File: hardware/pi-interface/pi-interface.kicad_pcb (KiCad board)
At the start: 2 copper layers, 8 parts, among them J1 RasPI_IO_Header, P1 SL030 RFID, P2 Molex HDD Power, P3 Door Solenoid, Q1 BC237

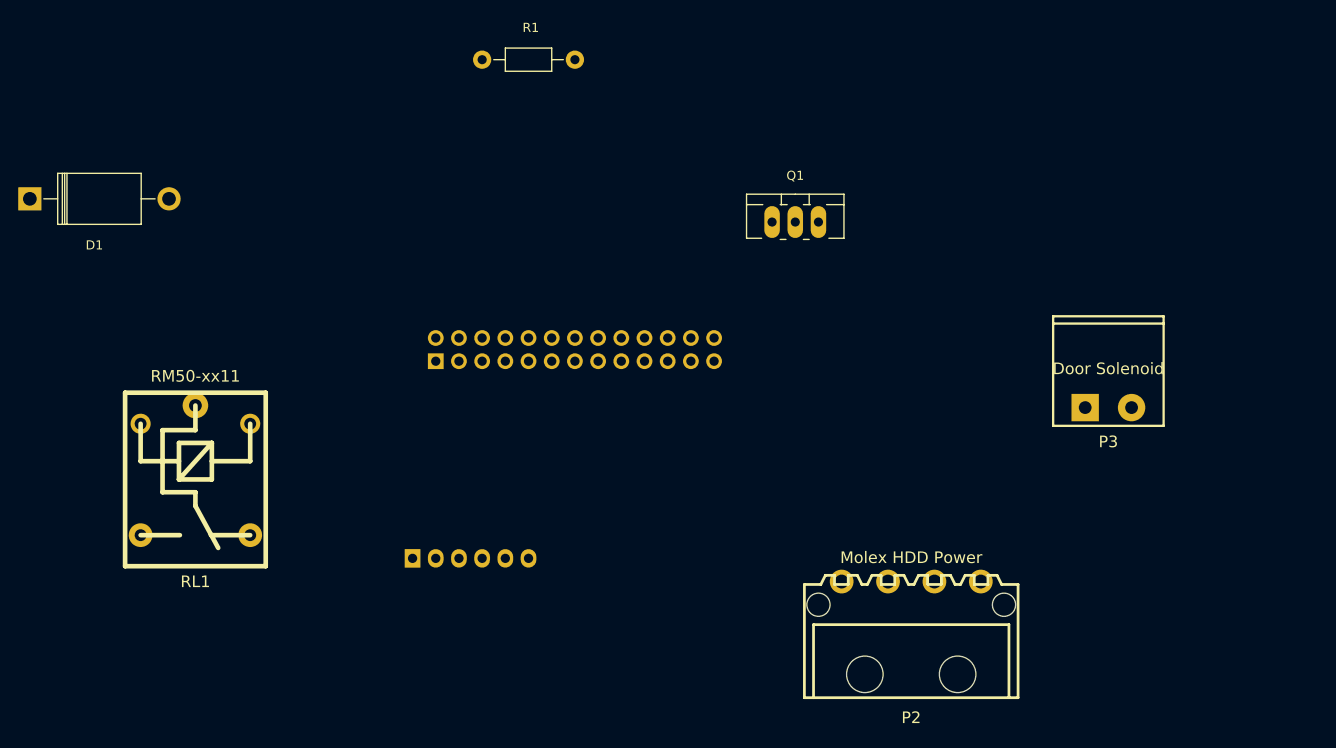
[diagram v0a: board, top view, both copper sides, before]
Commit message: Improved PCB, still needs checking against parts ordered
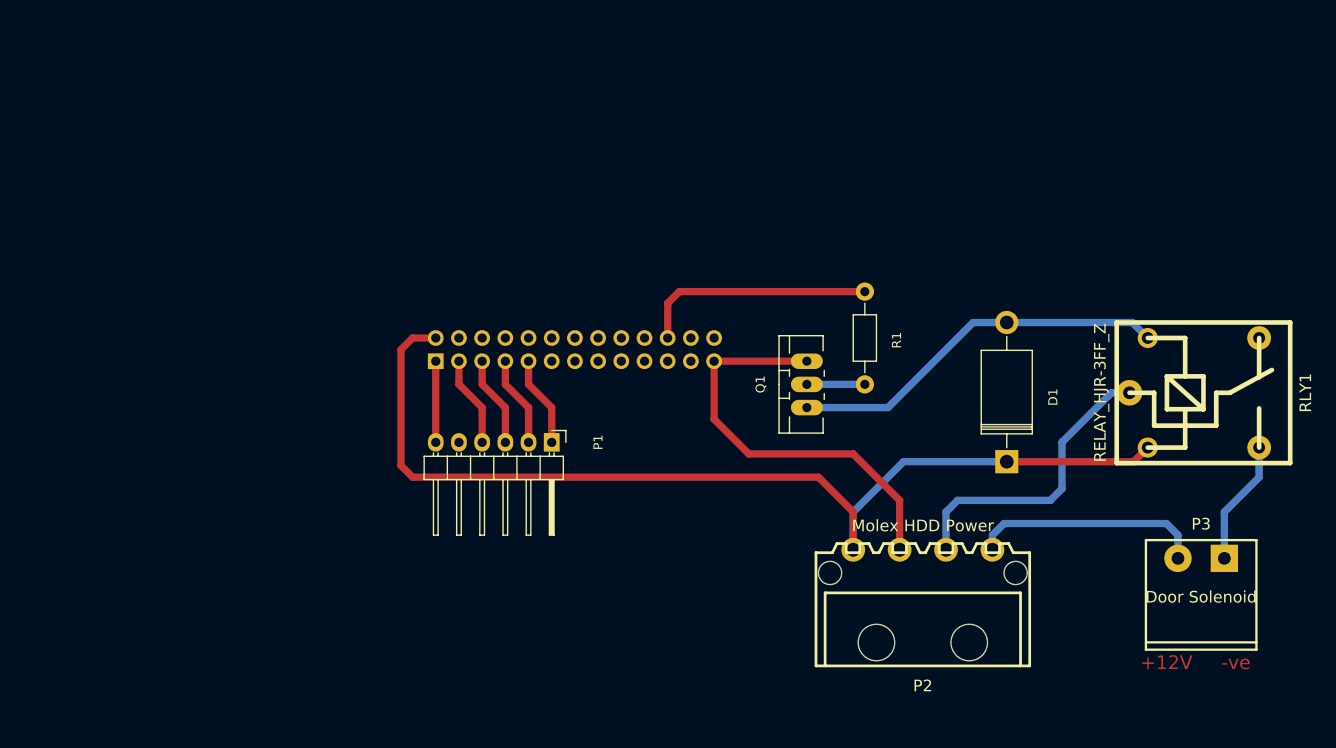
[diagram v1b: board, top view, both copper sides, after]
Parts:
- removed RL1: RM50-xx11, w_relay:relay_hjr-3ff_z
- added RLY1: RELAY_HJR-3FF_Z, w_relay:relay_hjr-3ff_z, F.Cu at (251.7, 98.7)
- P1: moved to F.Cu
- R1: value R -> 220R
- moved D1 110.8 mm to (230.2, 106.3), turned to 90 degrees
- moved R1 47.8 mm to (214.6, 92.7), turned to 270 degrees
- moved P1 19.8 mm to (180.3, 104.1)
- moved P3 19.4 mm to (251.5, 116.8), turned to 180 degrees
- moved Q1 17.8 mm to (208.3, 97.8), turned to 90 degrees
- moved P2 3.70 mm to (221.0, 121.9)
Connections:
- P1 pad 1: Net-(J1-Pad1) -> Net-(J1-Pad9)
- P1 pad 2: Net-(P1-Pad2) -> Net-(J1-Pad7)
- P1 pad 3: Net-(J1-Pad3) -> Net-(J1-Pad5)
- P1 pad 4: Net-(J1-Pad5) -> Net-(J1-Pad3)
- P1 pad 5: Net-(J1-Pad7) -> Net-(P1-Pad5)
- P1 pad 6: Net-(J1-Pad9) -> Net-(J1-Pad1)
- P2 pad 2: Net-(J1-Pad6) -> Net-(J1-Pad25)
- P3 pad 1: Net-(P2-Pad4) -> Net-(P3-Pad1)
- P3 pad 2: Net-(P3-Pad2) -> Net-(P2-Pad4)
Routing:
- net Net-(D1-Pad1): track 0.00 -> 112.1 mm
- net Net-(J1-Pad25): track 0.00 -> 45.9 mm
- net Net-(D1-Pad2): track 0.00 -> 41.9 mm
- net Net-(P2-Pad3): track 0.00 -> 32.6 mm
- net Net-(J1-Pad22): track 0.00 -> 25.9 mm
- net Net-(P2-Pad4): track 0.00 -> 25.5 mm
- net Net-(P3-Pad1): track 0.00 -> 13.7 mm
- net Net-(J1-Pad7): track 0.00 -> 9.94 mm
- net Net-(J1-Pad9): track 0.00 -> 9.94 mm
- net Net-(J1-Pad5): track 0.00 -> 9.94 mm
- net Net-(J1-Pad3): track 0.00 -> 9.94 mm
- net Net-(J1-Pad1): track 0.00 -> 8.89 mm
- net Net-(Q1-Pad2): track 0.00 -> 6.35 mm
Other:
- net class Default: trace_width 0.25 -> 0.8; via_dia 0.6 -> 1.6; via_drill 0.4 -> 1
- board text added: "+12V"
- board text added: "-ve"

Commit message: First finished (fingers crossed) PCB design.
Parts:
- P2: footprint w_conn_pc:conn_hdd_15-24-4441 -> w_conn_screw:mstbva_2,5%2f4-g-5,08
- moved P2 181.3 mm to (62.2, 34.3)
- moved D1 178.9 mm to (71.4, 23.7)
- moved J1 178.9 mm to (8.89, 12.7)
- moved P1 178.9 mm to (21.6, 21.6)
- moved P3 178.9 mm to (92.7, 34.3)
- moved Q1 178.9 mm to (49.5, 15.2)
- moved R1 178.9 mm to (55.9, 10.2)
- moved RLY1 178.9 mm to (93.0, 16.2)
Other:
- board outline added: 106.7 x 47 mm
- board text added: "DoES Liverpool Doorbot r20150910"

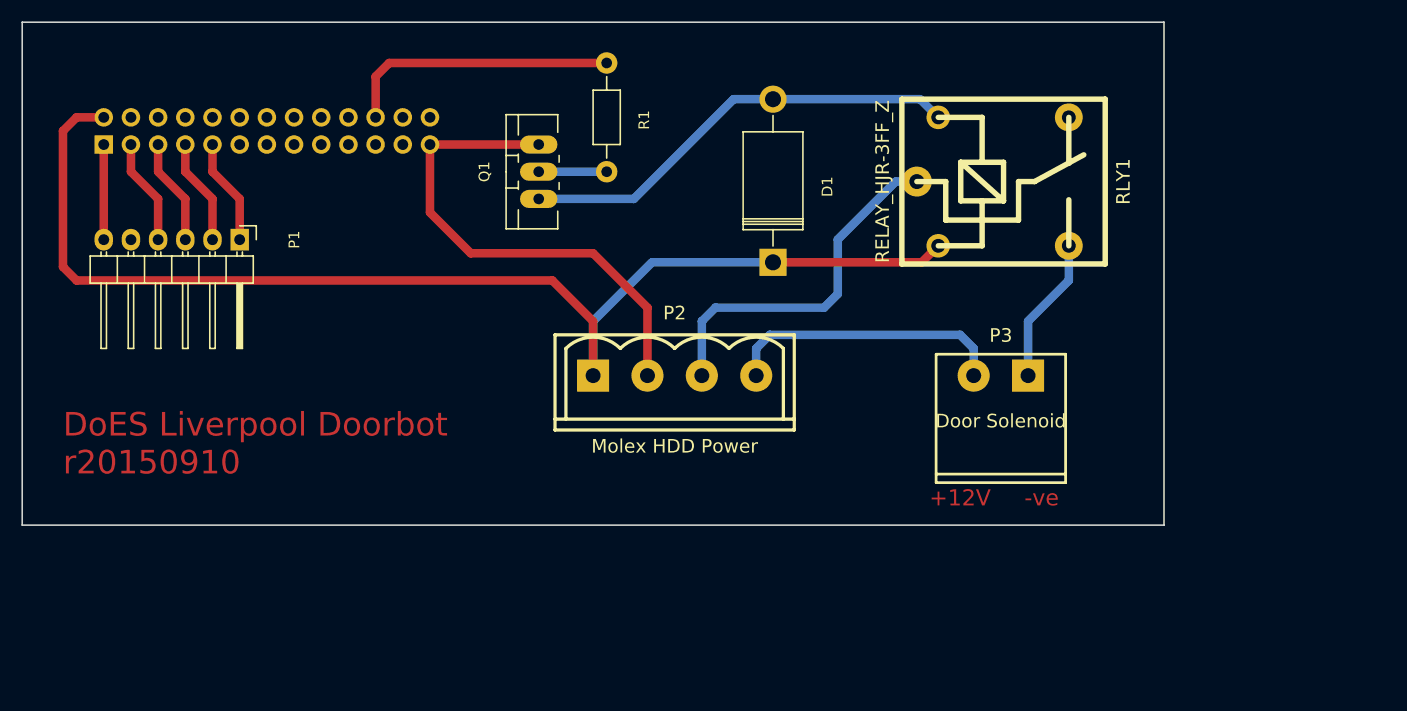
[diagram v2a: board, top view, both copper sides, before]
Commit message: I2S DAC added to PCB.  Fixes #17
Also added DoES Liverpool logo to silkscreen, and other mods for the first revision of the PCB sent to be manufactured.
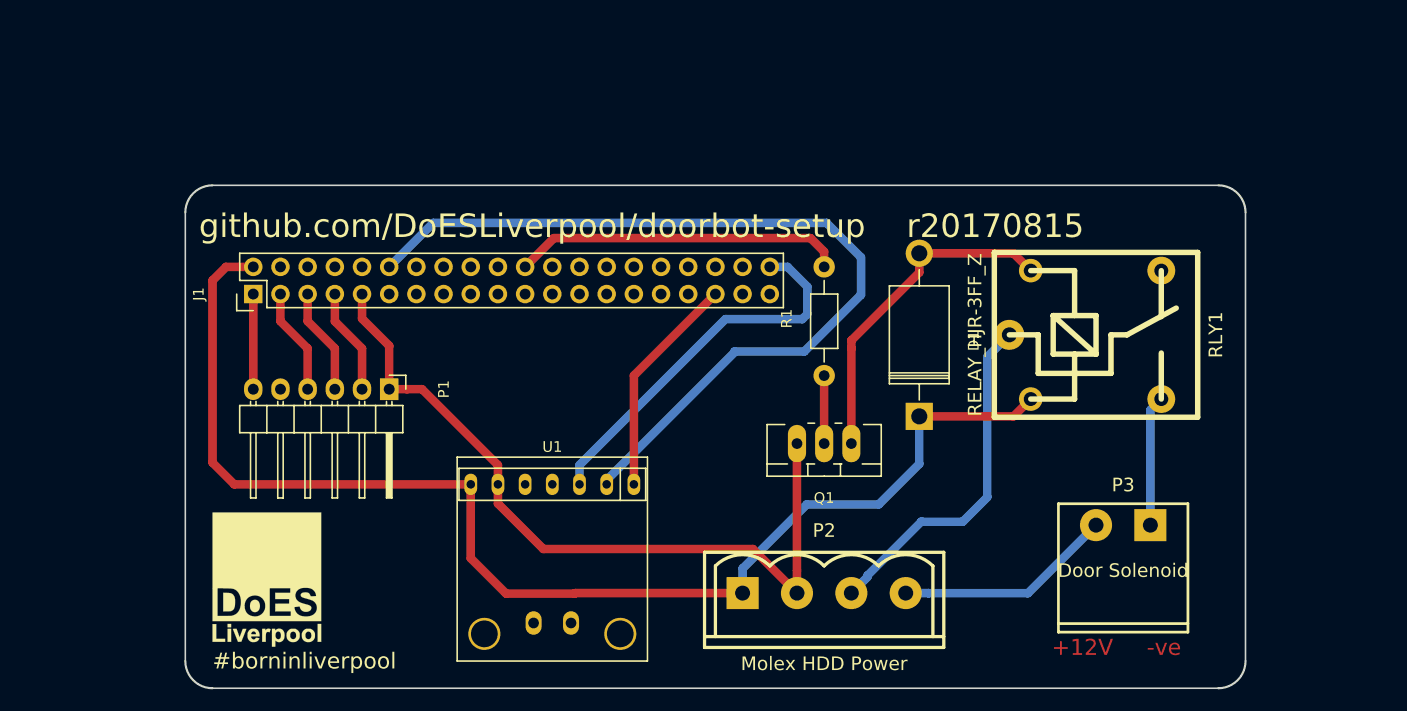
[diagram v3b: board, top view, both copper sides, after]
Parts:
- added G***: LOGO, pi-interface:DoESLiverpool-logo, F.Cu at (24.1, 53.3)
- added U1: MAX98357A-Breakout, MCQN Ltd:MAX98357-Breakout, F.Cu at (50.8, 44.5)
- J1: value RasPI_IO_Header -> Raspberry_Pi_2_3; footprint Socket_Strips:Socket_Strip_Straight_2x13 -> Pin_Headers:Pin_Header_Straight_2x20; moved to F.Cu
- moved Q1 36.8 mm to (76.2, 40.6), turned to 180 degrees
- moved R1 27.9 mm to (76.2, 29.2), turned to 90 degrees
- moved P2 24.7 mm to (76.2, 54.6)
- moved D1 19.8 mm to (85.1, 38.1)
- moved P1 19.8 mm to (35.6, 35.6)
- moved J1 19.8 mm to (22.9, 26.7), turned to 90 degrees
- moved P3 18.1 mm to (104.1, 48.3)
- moved RLY1 16.7 mm to (101.6, 30.5)
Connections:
- P2 pad 2: Net-(J1-Pad25) -> Net-(J1-Pad9)
- Q1 pad 3: Net-(J1-Pad25) -> Net-(J1-Pad9)
- R1 pad 1: Net-(J1-Pad22) -> Net-(Q1-Pad2)
- R1 pad 2: Net-(Q1-Pad2) -> Net-(J1-Pad22)
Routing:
- net Net-(J1-Pad12): track 0.00 -> 82.0 mm
- net Net-(J1-Pad9): track 9.94 -> 72.0 mm
- net Net-(J1-Pad25): track 45.9 -> 0.00 mm
- net Net-(J1-Pad40): track 0.00 -> 35.8 mm
- net Net-(J1-Pad35): track 0.00 -> 20.9 mm
- net Net-(D1-Pad2): track 41.9 -> 31.5 mm
- net Net-(D1-Pad1): track 112.1 -> 118.4 mm
- net Net-(P2-Pad4): track 25.5 -> 20.4 mm
- net Net-(J1-Pad22): track 25.9 -> 31.0 mm
- net Net-(P3-Pad1): track 13.7 -> 12.2 mm
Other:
- board size 106.7 x 47 mm -> 99.1 x 47 mm
- net class Default: clearance 0.2 -> 0
- rule trace_clearance: 0.2 -> 0
- board text added: "#borninliverpool"
- board text added: "github.com/DoESLiverpool/doorbot-setup r20170815"
- board text removed: "DoES Liverpool Doorbot r20150910"

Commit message: Enlarge holes for the Molex connector.  Fixes #21
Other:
- net class Default: trace_width 0.8 -> 0.25
- board text added: "github.com/DoESLiverpool/doorbot-setup r20170905"
- board text removed: "github.com/DoESLiverpool/doorbot-setup r20170815"
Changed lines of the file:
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@@
-(kicad_pcb (version 20170123) (host pcbnew no-vcs-found-7ab6368~59~ubuntu16.04.1)
+(kicad_pcb (version 20170123) (host pcbnew no-vcs-found-1fe91e6~59~ubuntu16.04.1)
   (general
     (thickness 1.6)
@@
   )
   (setup
-    (last_trace_width 0.8)
+    (last_trace_width 0.25)
     (trace_clearance 0)
     (zone_clearance 0.508)
@@
     (mod_text_size 1 1)
     (mod_text_width 0.15)
-    (pad_size 1.524 1.524)
-    (pad_drill 0.762)
+    (pad_size 2.99974 2.99974)
+    (pad_drill 1.55)
     (pad_to_mask_clearance 0.2)
     (aux_axis_origin 16.51 63.5)
@@
       (layerselection 0x010ff_ffffffff)
       (usegerberextensions true)
+      (usegerberattributes true)
+      (usegerberadvancedattributes true)
+      (creategerberjobfile true)
       (excludeedgelayer true)
       (linewidth 0.100000)
@@
   (net_class Default "This is the default net class."
     (clearance 0)
-    (trace_width 0.8)
+    (trace_width 0.25)
     (via_dia 1.6)
     (via_drill 1)
@@
     (fp_arc (start 2.54 0) (end 0 -2.54) (angle 90) (layer F.SilkS) (width 0.3048))
     (fp_arc (start 7.62 0) (end 5.08 -2.54) (angle 90) (layer F.SilkS) (width 0.3048))
-    (pad 1 thru_hole rect (at -7.62 0) (size 2.99974 2.99974) (drill 1.39954) (layers *.Cu *.Mask F.SilkS)
+    (pad 1 thru_hole rect (at -7.62 0) (size 2.99974 2.99974) (drill 1.55) (layers *.Cu *.Mask F.SilkS)
       (net 26 "Net-(D1-Pad1)"))
-    (pad 4 thru_hole circle (at 7.62 0) (size 2.99974 2.99974) (drill 1.39954) (layers *.Cu *.Mask F.SilkS)
+    (pad 4 thru_hole circle (at 7.62 0) (size 2.99974 2.99974) (drill 1.55) (layers *.Cu *.Mask F.SilkS)
       (net 25 "Net-(P2-Pad4)"))
-    (pad 3 thru_hole circle (at 2.54 0) (size 2.99974 2.99974) (drill 1.39954) (layers *.Cu *.Mask F.SilkS)
+    (pad 3 thru_hole circle (at 2.54 0) (size 2.99974 2.99974) (drill 1.55) (layers *.Cu *.Mask F.SilkS)
       (net 24 "Net-(P2-Pad3)"))
-    (pad 2 thru_hole circle (at -2.54 0) (size 2.99974 2.99974) (drill 1.39954) (layers *.Cu *.Mask F.SilkS)
+    (pad 2 thru_hole circle (at -2.54 0) (size 2.99974 2.99974) (drill 1.55) (layers *.Cu *.Mask F.SilkS)
       (net 7 "Net-(J1-Pad9)"))
     (model walter/conn_screw/mstbva_2,5-4-g-5,08.wrl
@@
     (effects (font (size 1.5 1.5) (thickness 0.3)) (justify left))
   )
-  (gr_text "github.com/DoESLiverpool/doorbot-setup    r20170815" (at 17.78 20.32) (layer F.SilkS)
+  (gr_text "github.com/DoESLiverpool/doorbot-setup    r20170905" (at 17.78 20.32) (layer F.SilkS)
     (effects (font (size 2.2 2.2) (thickness 0.3)) (justify left))
   )
@@
   (gr_line (start 19.05 63.5) (end 113.03 63.5) (layer Edge.Cuts) (width 0.15))
   (gr_line (start 16.51 19.05) (end 16.51 60.96) (layer Edge.Cuts) (width 0.15))
-  (gr_text -ve (at 107.95 59.69) (layer F.Cu)
+  (gr_text -ve (at 107.95 59.69) (layer F.SilkS)
     (effects (font (size 1.5 1.5) (thickness 0.3)))
   )
-  (gr_text +12V (at 100.33 59.69) (layer F.Cu)
+  (gr_text +12V (at 100.33 59.69) (layer F.SilkS)
     (effects (font (size 1.5 1.5) (thickness 0.3)))
   )
